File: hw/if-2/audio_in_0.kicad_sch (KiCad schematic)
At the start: 33 parts, among them U41 TL072, U42 TL072

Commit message: Documentation improvements, moved a OVP circuit
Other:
- title: COS/CTCSS/PTT Controls (Radio 0) -> Audio Input (Radio 0)
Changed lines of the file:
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@@
 	(paper "USLetter")
 	(title_block
-		(title "COS/CTCSS/PTT Controls (Radio 0)")
-		(date "2025-05-13")
+		(title "Audio Input (Radio 0)")
+		(date "2025-05-31")
 		(rev "2")
 		(company "Bruce MacKinnon KC1FSZ")

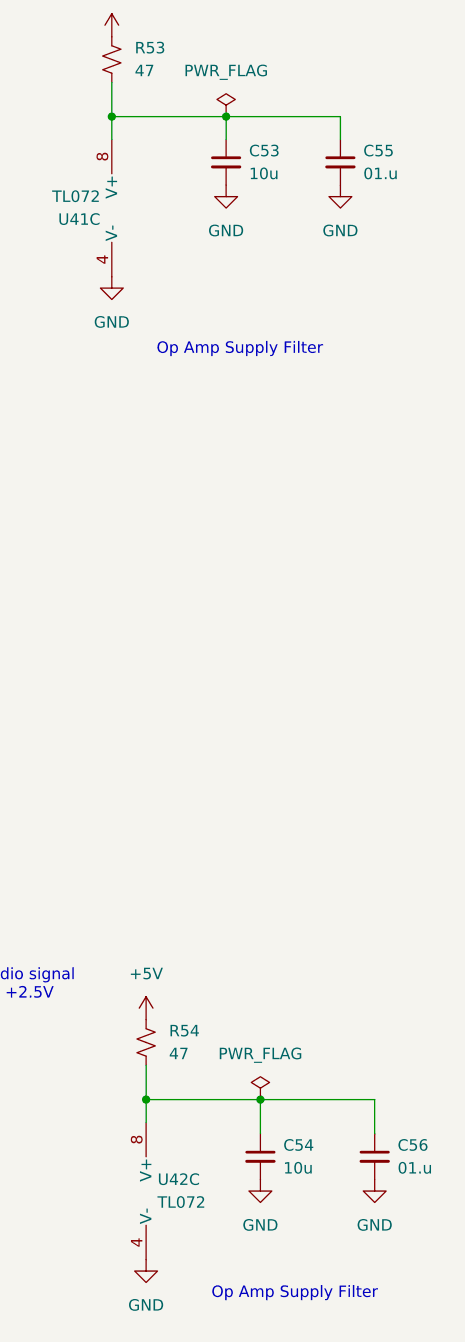
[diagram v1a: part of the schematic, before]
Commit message: Added audio clip
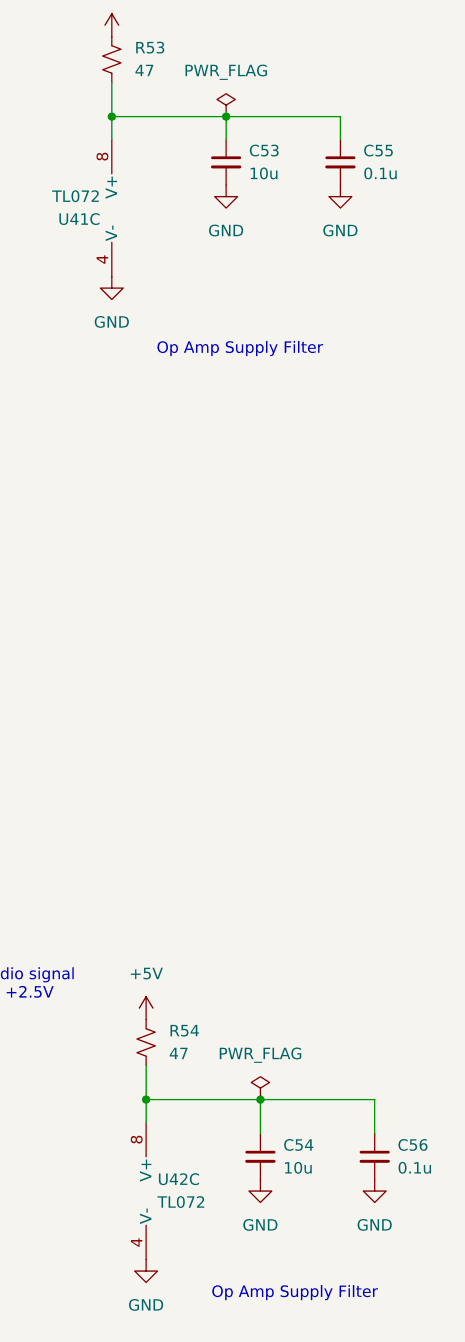
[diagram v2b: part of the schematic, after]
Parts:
- C55, C56: value 01.u -> 0.1u
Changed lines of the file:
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@@
 			)
 		)
-		(property "Value" "01.u"
+		(property "Value" "0.1u"
 			(at 259.08 148.5962 0)
 			(effects
@@
 			)
 		)
-		(property "Value" "01.u"
+		(property "Value" "0.1u"
 			(at 255.27 38.1062 0)
 			(effects

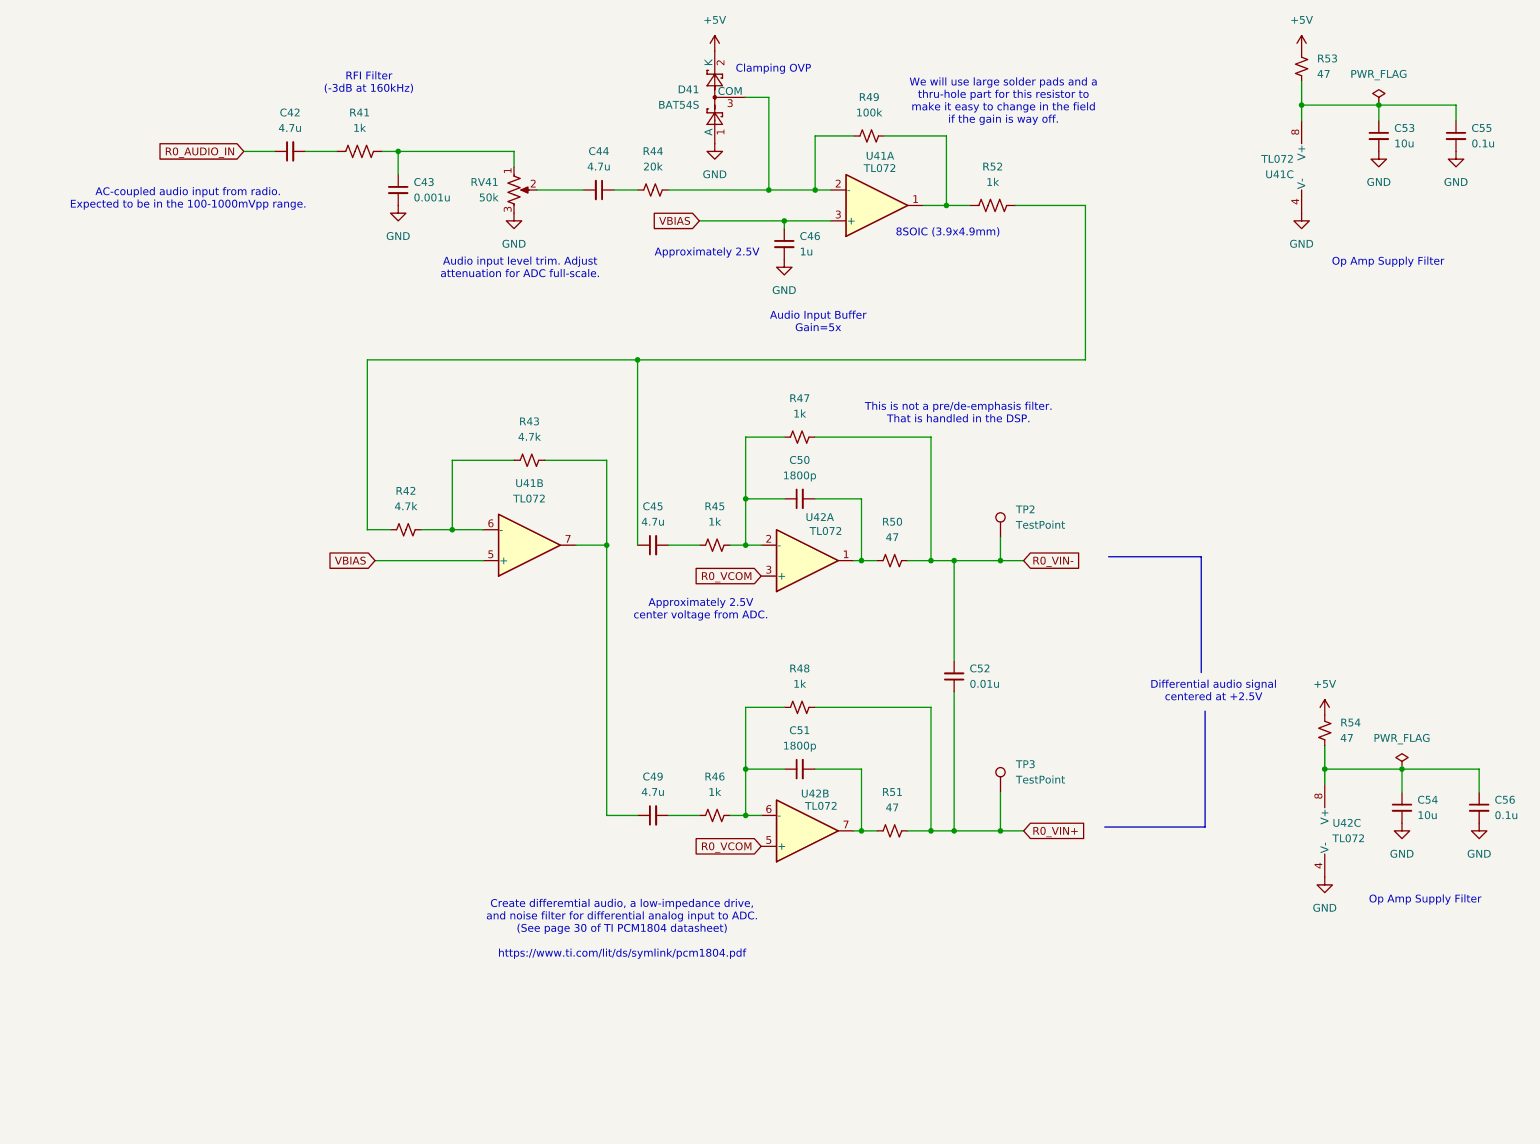
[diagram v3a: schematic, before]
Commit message: Updated audio file to 16K
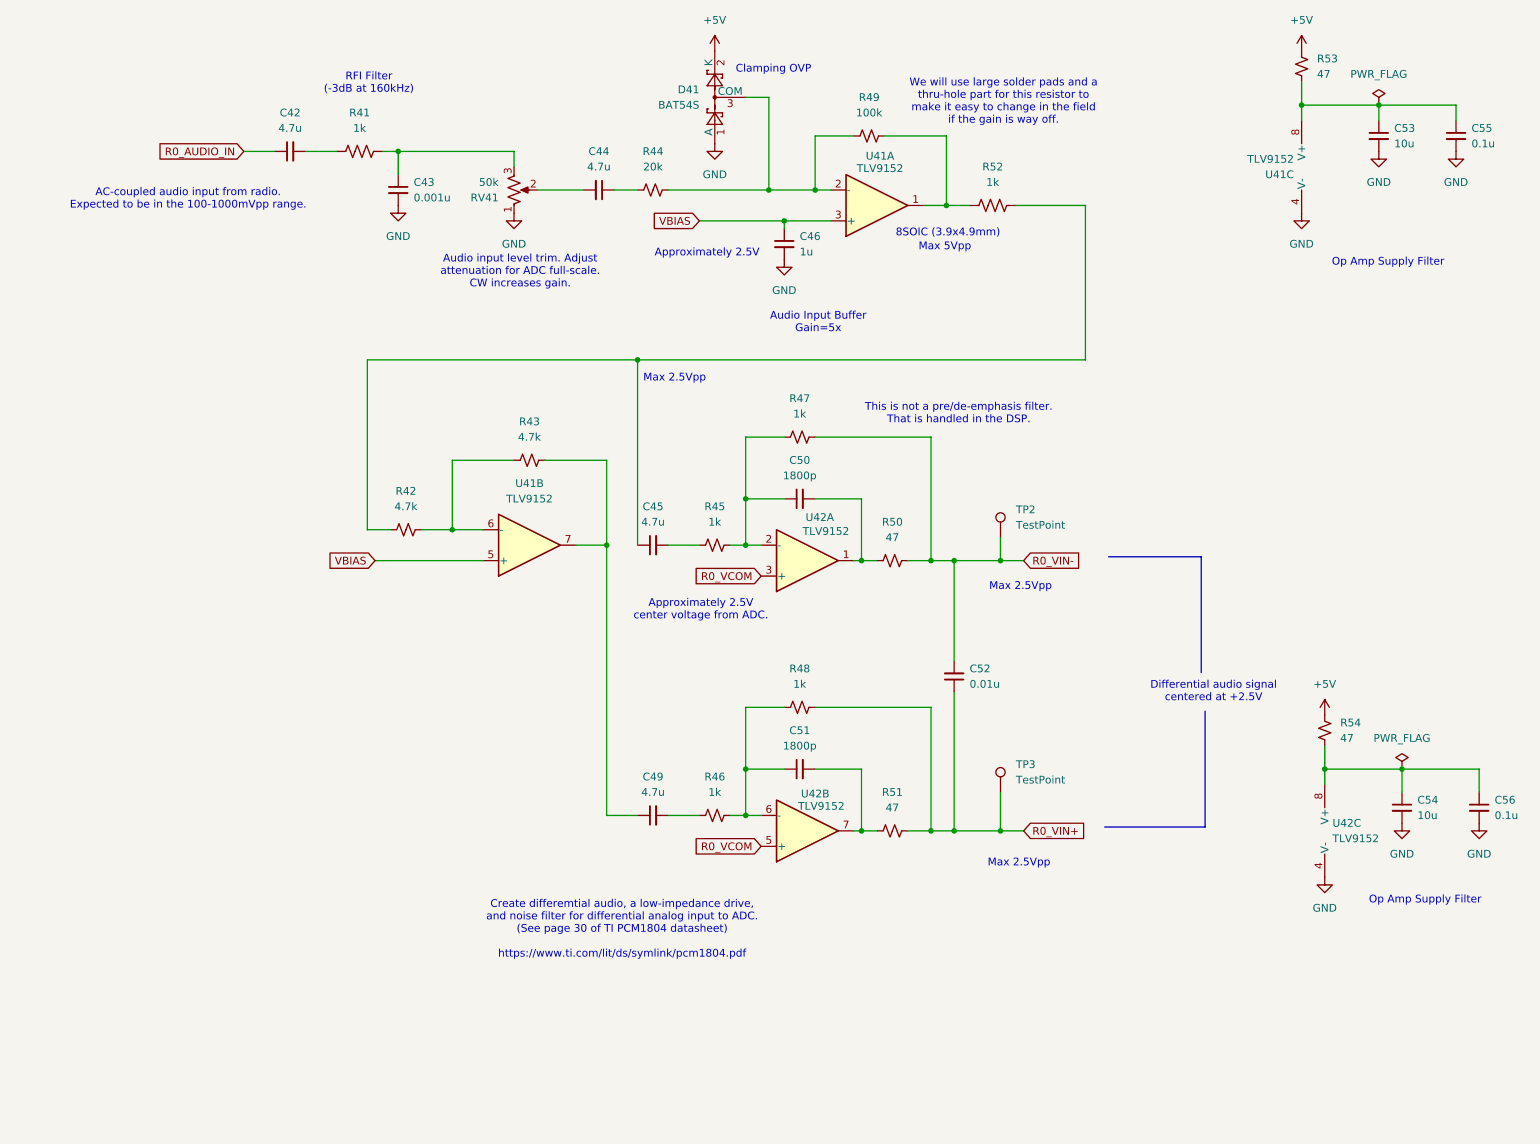
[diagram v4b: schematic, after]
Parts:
- R49: footprint Resistor_SMD:R_0805_2012Metric_Pad1.20x1.40mm_HandSolder -> Resistor_THT:R_Axial_DIN0516_L15.5mm_D5.0mm_P5.08mm_Vertical
- U41, U42: value TL072 -> TLV9152
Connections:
- net GND: now also RV41.1; no longer RV41.3
- net at C43.1, R41.2: now also RV41.3; no longer RV41.1
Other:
- note added: "Audio input level trim. Adjust attenuation for ADC full-scale. CW increases gain."
- note added: "Max 2.5Vpp"
- note added: "Max 5Vpp"
- note removed: "Audio input level trim. Adjust attenuation for ADC full-scale."
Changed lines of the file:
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@@
 		)
 	)
-	(text "Audio input level trim. Adjust\nattenuation for ADC full-scale."
+	(text "Max 2.5Vpp"
 		(exclude_from_sim no)
-		(at 98.806 58.674 0)
+		(at 124.206 76.708 0)
 		(effects
 			(font
 				(size 1.27 1.27)
+				(color 254 69 255 1)
+			)
+		)
+	)
+	(text "Max 2.5Vpp"
+		(exclude_from_sim no)
+		(at 180.848 156.464 0)
+		(effects
+			(font
+				(size 1.27 1.27)
+				(color 254 69 255 1)
+			)
+		)
+	)
+	(text "Audio input level trim. Adjust\nattenuation for ADC full-scale.\nCW increases gain."
+		(exclude_from_sim no)
+		(at 98.806 59.182 0)
+		(effects
+			(font
+				(size 1.27 1.27)
+			)
+		)
+	)
+	(text "Max 5Vpp"
+		(exclude_from_sim no)
+		(at 168.656 55.118 0)
+		(effects
+			(font
+				(size 1.27 1.27)
+				(color 254 69 255 1)
 			)
 		)
@@
 		)
 	)
+	(text "Max 2.5Vpp"
+		(exclude_from_sim no)
+		(at 181.102 110.998 0)
+		(effects
+			(font
+				(size 1.27 1.27)
+				(color 254 69 255 1)
+			)
+		)
+	)
 	(text "AC-coupled audio input from radio. \nExpected to be in the 100-1000mVpp range."
 		(exclude_from_sim no)
@@
 			)
 		)
-		(property "Value" "TL072"
+		(property "Value" "TLV9152"
 			(at 149.098 101.854 0)
 			(effects
@@
 			)
 		)
-		(property "Value" "TL072"
+		(property "Value" "TLV9152"
 			(at 232.41 152.3999 0)
 			(effects
@@
 			)
 		)
-		(property "Footprint" "Resistor_SMD:R_0805_2012Metric_Pad1.20x1.40mm_HandSolder"
+		(property "Footprint" "Resistor_THT:R_Axial_DIN0516_L15.5mm_D5.0mm_P5.08mm_Vertical"
 			(at 156.21 36.83 0)
 			(effects
@@
 			)
 		)
-		(property "Value" "TL072"
+		(property "Value" "TLV9152"
 			(at 148.336 147.066 0)
 			(effects
@@
 			)
 		)
-		(property "Value" "TL072"
+		(property "Value" "TLV9152"
 			(at 157.988 42.164 0)
 			(effects
@@
 			)
 		)
-		(property "Value" "TL072"
+		(property "Value" "TLV9152"
 			(at 226.06 40.6401 0)
 			(effects
@@
 		(lib_id "Device:R_Potentiometer_US")
 		(at 97.79 45.72 0)
+		(mirror x)
 		(unit 1)
 		(exclude_from_sim no)
@@
 		(on_board yes)
 		(dnp no)
-		(fields_autoplaced yes)
 		(property "Reference" "RV41"
-			(at 95.25 44.4499 0)
+			(at 95.25 46.9901 0)
 			(effects
 				(font
@@
 		)
 		(property "Value" "50k"
-			(at 95.25 46.9899 0)
+			(at 95.25 44.4501 0)
 			(effects
 				(font
@@
 			)
 		)
-		(property "Value" "TL072"
+		(property "Value" "TLV9152"
 			(at 100.33 96.52 0)
 			(effects

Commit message: Updating schematics, create new mini-board for radio interface
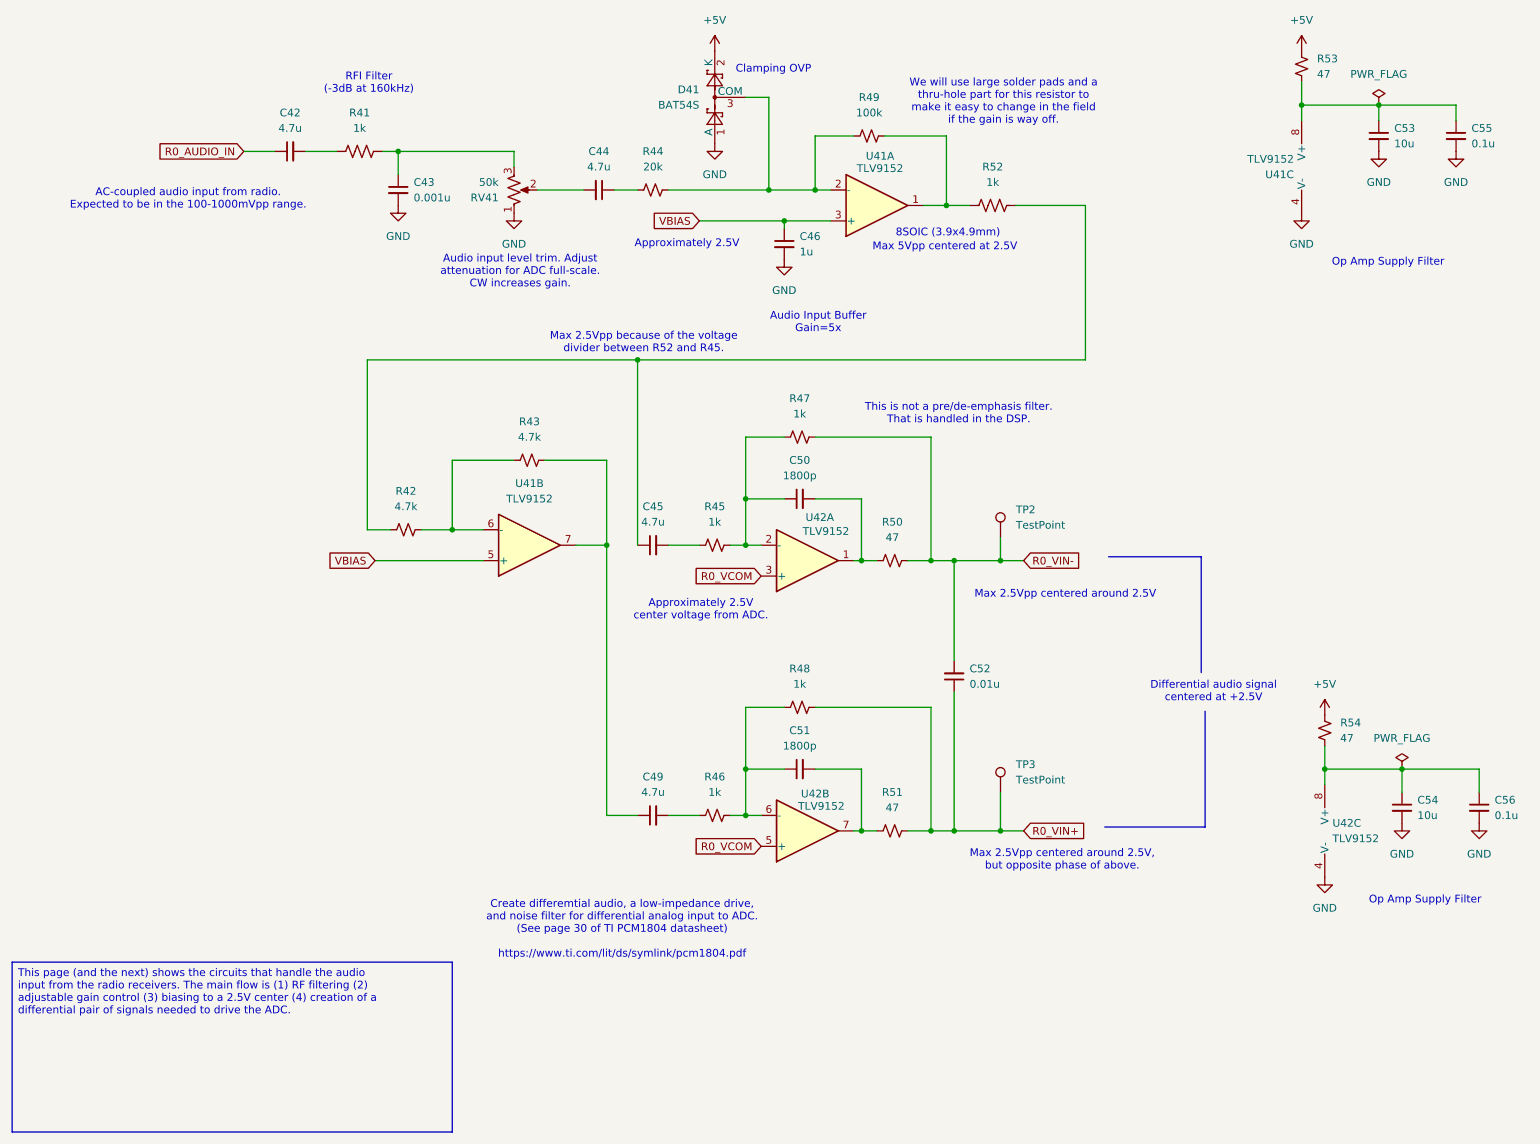
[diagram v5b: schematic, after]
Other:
- note added: "Max 2.5Vpp because of the voltage divider between R52 and R45."
- note added: "Max 2.5Vpp centered around 2.5V"
- note added: "Max 2.5Vpp centered around 2.5V, but opposite phase of above."
- note added: "Max 5Vpp centered at 2.5V"
- note removed: "Max 2.5Vpp"
- note removed: "Max 5Vpp"
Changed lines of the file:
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@@
 			(font
 				(size 1.27 1.27)
+				(color 255 7 253 1)
 			)
 		)
@@
 			(font
 				(size 1.27 1.27)
+				(color 255 12 215 1)
 			)
 		)
@@
 		)
 	)
-	(text "Max 2.5Vpp"
+	(text "Max 2.5Vpp because of the voltage \ndivider between R52 and R45."
 		(exclude_from_sim no)
-		(at 124.206 76.708 0)
-		(effects
-			(font
-				(size 1.27 1.27)
-				(color 254 69 255 1)
-			)
-		)
-	)
-	(text "Max 2.5Vpp"
-		(exclude_from_sim no)
-		(at 180.848 156.464 0)
+		(at 119.126 70.866 0)
 		(effects
 			(font
@@
 		)
 	)
-	(text "Max 5Vpp"
+	(text "Max 5Vpp centered at 2.5V"
 		(exclude_from_sim no)
 		(at 168.656 55.118 0)
@@
 			(font
 				(size 1.27 1.27)
+			)
+		)
+	)
+	(text "Max 2.5Vpp centered around 2.5V,\nbut opposite phase of above."
+		(exclude_from_sim no)
+		(at 187.96 155.956 0)
+		(effects
+			(font
+				(size 1.27 1.27)
+				(color 254 69 255 1)
 			)
 		)
@@
 		)
 	)
-	(text "Max 2.5Vpp"
+	(text "Max 2.5Vpp centered around 2.5V"
 		(exclude_from_sim no)
-		(at 181.102 110.998 0)
+		(at 188.468 112.268 0)
 		(effects
 			(font
@@
 	(text "Approximately 2.5V\n"
 		(exclude_from_sim no)
-		(at 129.54 56.134 0)
+		(at 126.238 54.61 0)
 		(effects
 			(font
 				(size 1.27 1.27)
+				(color 255 14 229 1)
 			)
 		)
@@
 		)
 	)
+	(text_box "This page (and the next) shows the circuits that handle the audio input from the radio receivers. The main flow is (1) RF filtering (2) adjustable gain control (3) biasing to a 2.5V center (4) creation of a differential pair of signals needed to drive the ADC.\n"
+		(exclude_from_sim no)
+		(at 15.24 172.72 0)
+		(size 72.39 27.94)
+		(margins 0.9525 0.9525 0.9525 0.9525)
+		(stroke
+			(width 0)
+			(type solid)
+		)
+		(fill
+			(type color)
+			(color 205 245 255 1)
+		)
+		(effects
+			(font
+				(size 1.27 1.27)
+			)
+			(justify left top)
+		)
+	)
